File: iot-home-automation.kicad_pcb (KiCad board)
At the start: 4 copper layers, 53.2 x 41.6 mm, 26 parts, among them J1 Conn_01x05_Pin, J2 Conn_01x08_Pin, J3 Conn_01x02_Pin, J4 Conn_02x08_Odd_Even, Q1 PMOS, SW1 SW_Push_SPDT, U1 STM32WB5MMGH6TR, U2 SHTC3, U3 TPS62202DBV, U4 OPT3001DNPT

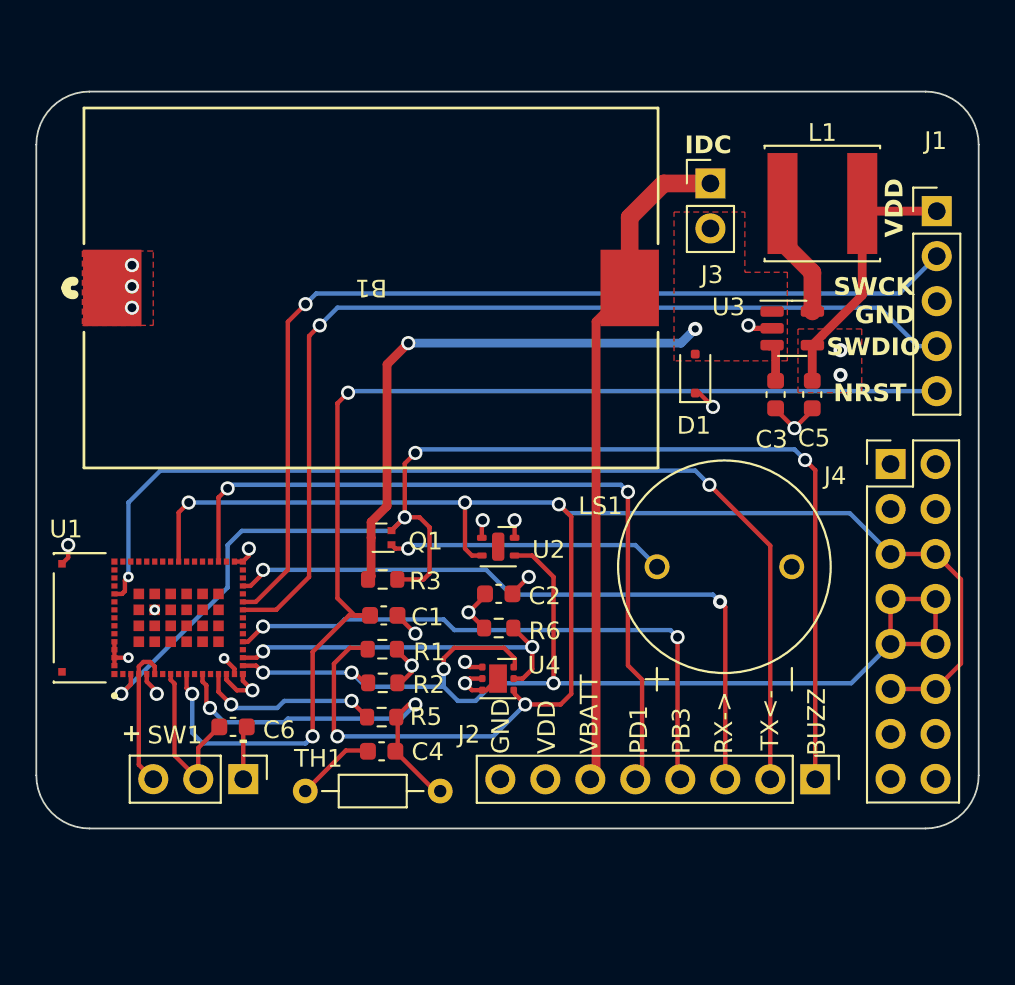
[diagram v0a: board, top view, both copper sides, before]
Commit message: Schematic and first routing pass done
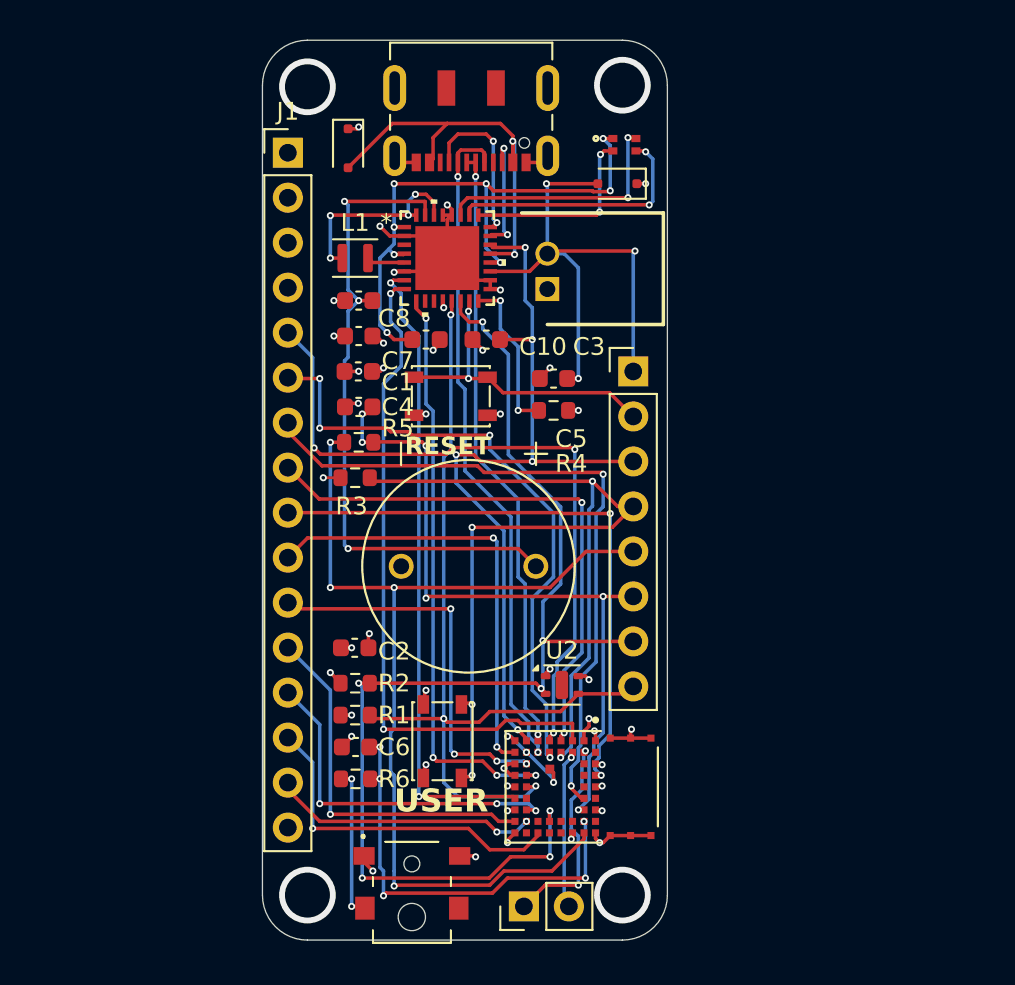
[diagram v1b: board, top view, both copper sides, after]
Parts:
- removed B1: BU2032SM-JJ-GTR, BU2032SM-JJ-GTR:BU2032SM-JJ-GTR_MPD
- removed J4: Conn_02x08_Odd_Even, Connector_PinHeader_2.54mm:PinHeader_2x08_P2.54mm_Vertical
- removed Q1: PMOS, Package_TO_SOT_SMD:SOT-723
- removed TH1: 3.3K@25C, Resistor_THT:R_Axial_DIN0204_L3.6mm_D1.6mm_P7.62mm_Horizontal
- removed U1: STM32WB5MMGH6TR, STM32WB5MMGH6TR:XCVR_STM32WB5MMGH6TR
- added C10: 10uF, Capacitor_SMD:C_0603_1608Metric, F.Cu at (140.8, 97.0)
- added C7: 0.1uF, Capacitor_SMD:C_0603_1608Metric, F.Cu at (137.0, 96.8)
- added C8: 1uF, Capacitor_SMD:C_0603_1608Metric, F.Cu at (137.0, 94.8)
- added D2: D_TVS, Diode_SMD:D_SOD-323F, F.Cu at (151.6, 88.2)
- added J5: Conn_01x02_Pin, Connector_PinHeader_2.54mm:PinHeader_1x02_P2.54mm_Vertical, F.Cu at (146.3, 129.0)
- added J6: Conn_01x08_Pin, Connector_PinHeader_2.54mm:PinHeader_1x08_P2.54mm_Vertical, F.Cu at (152.5, 98.8)
- added LED1: APHF1608LSEEQBDZGKC, ul_APHF1608LSEEQBDZGKC:APHF_KNB, F.Cu at (152.0, 86.0)
- added R4: 330K, Resistor_SMD:R_0603_1608Metric, F.Cu at (148.0, 101.0)
- added SW2: SW_Push, Button_Switch_SMD:SW_SPST_PTS810, F.Cu at (142.2, 100.2)
- added SW3: SW_Push, Button_Switch_SMD:SW_SPST_PTS810, F.Cu at (141.7, 119.7)
- C1: value 100nF -> 10uF
- C3: value 10u -> 1uF
- C4, C6: value 0.1u -> 100nF
- C5: value 10u -> 2.2uF
- J1: value Conn_01x05_Pin -> Conn_01x16_Female; footprint Connector_PinHeader_2.54mm:PinHeader_1x05_P2.54mm_Vertical -> Connector_PinHeader_2.54mm:PinHeader_1x16_P2.54mm_Vertical
- J2: value Conn_01x08_Pin -> USB_C_Receptacle_USB2.0_16P; footprint Connector_PinHeader_2.54mm:PinHeader_1x08_P2.54mm_Vertical -> Connector_USB:USB_C_Receptacle_JAE_DX07S016JA1R1500
- J3: value Conn_01x02_Pin -> 440055-2; footprint Connector_PinHeader_2.54mm:PinHeader_1x02_P2.54mm_Vertical -> jst:SHDRRA2W50P0X200_1X2_600X770X525P
- L1: value 10u -> 2.2uH; footprint Inductor_SMD:L_Changjiang_FNR6028S -> Inductor_SMD:L_Murata_DFE201610P
- R3: value 220K -> 10K
- R6: value 10K -> 200k
- SW1: footprint Connector_PinHeader_2.54mm:PinHeader_1x03_P2.54mm_Vertical -> CL-DA-1BB4-A2T:CLDA1BB4A2T
- U3: value TPS62202DBV -> 453-00059R; footprint Package_TO_SOT_SMD:SOT-23-5 -> 453-00059R:XCVR_453-00059R
- U4: value OPT3001DNPT -> NPM1300-QEAA-R7; footprint Package_SON:WSON-6-1EP_2x2mm_P0.65mm_EP1x1.6mm -> ul_NPM1300-QEAA-R7:QFN32_5X5_NOR
- moved J2 42.6 mm to (143.3, 84.0), turned to 180 degrees
- moved J1 36.8 mm to (133.0, 86.5)
- moved U3 28.5 mm to (149.6, 122.2), turned to -90 degrees
- moved L1 26.6 mm to (136.8, 92.4)
- moved U4 23.9 mm to (142.0, 92.4)
- moved D1 23.4 mm to (136.4, 86.2), turned to -90 degrees
- moved C4 19.5 mm to (137.0, 100.8)
- moved C3 16.6 mm to (144.2, 97.0), turned to 180 degrees
- moved R5 15.6 mm to (137.0, 102.8)
- moved C5 14.6 mm to (148.0, 99.2), turned to 180 degrees
- moved LS1 14.4 mm to (143.2, 109.8), turned to -90 degrees
- moved C1 13.8 mm to (137.0, 98.8), turned to 180 degrees
- moved R6 11.7 mm to (136.8, 121.8)
- moved SW1 11.5 mm to (140.0, 128.2), turned to 90 degrees
- moved J3 11.0 mm to (147.7, 94.2), turned to -90 degrees
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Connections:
- C1 pad 1: /NRST -> 3V3
- C2 pad 1: VDD -> 3V3
- C3 pad 1: VCC -> VBUSOUT
- C4 pad 1: /Vtherm -> /VTH
- C5 pad 1: VDD -> VBAT
- C6 pad 1: /Door_EXTI -> /Door_IRQ
- D1 pad 2: VCC -> VBUSIN
- J1 pad 1: VDD -> GND
- J1 pad 2: /SWCLK -> 3V3
- J1 pad 3: GND -> unconnected-(J1-Pin_3-Pad3)
- J1 pad 4: /SWDIO -> GND
- J1 pad 5: /NRST -> /IO14
- J3 pad 1: +BATT -> GND
- J3 pad 2: VCC -> VBAT
- L1 pad 1: Net-(U3-SW) -> 3V3
- L1 pad 2: VDD -> Net-(U4-SW2)
- LS1 pad P: Net-(Q1-D) -> /LSOUT2
- R1 pad 1: VDD -> 3V3
- R1 pad 2: /SCL1 -> /SDA
- R2 pad 1: VDD -> 3V3
- R2 pad 2: /SDA1 -> /SCL
- R3 pad 1: VCC -> 3V3
- R3 pad 2: /nBuzzer -> /USER_BTN
- R5 pad 1: /VDD_THERM -> /VDD_TH
- R5 pad 2: /Vtherm -> /VTH
- R6 pad 1: VDD -> Net-(SW1-B)
- R6 pad 2: /LIGHT_IRQ -> /Door_IRQ
- SW1 pad 2: /Door_EXTI -> Net-(SW1-B)
- SW1 pad 3: VDD -> 3V3
- U2 pad 1: VDD -> 3V3
- U2 pad 2: /SCL1 -> /SCL
- U2 pad 3: /SDA1 -> /SDA
- U3 pad 1: VCC -> GND
- U3 pad 2: GND -> unconnected-(U3-NC-Pad2)
- U3 pad 3: VCC -> GND
- U3 pad 4: VDD -> /IO24
- U3 pad 5: Net-(U3-SW) -> GND
- U4 pad 1: VDD -> VSYS
- U4 pad 3: GND -> unconnected-(U4-SW1-Pad3)
- U4 pad 4: /SCL1 -> VSYS
- U4 pad 5: /LIGHT_IRQ -> Net-(U4-SW2)
- U4 pad 6: /SDA1 -> GND
- U4 pad 7: GND -> /GPIO0
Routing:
- net /SCL1: track 94.7 -> 0.00 mm, vias 5 -> 0
- net /nBuzzer: track 74.6 -> 0.00 mm, vias 4 -> 0
- net /NRST: track 66.9 -> 0.00 mm, vias 3 -> 0
- net /SCL: track 0.00 -> 66.5 mm, vias 0 -> 7
- net /SDA1: track 65.4 -> 0.00 mm, vias 4 -> 0
- net /MCU_TX1: track 57.7 -> 0.00 mm, vias 2 -> 0
- net /USER_BTN: track 0.00 -> 56.9 mm, vias 0 -> 5
- net /VDD_TH: track 0.00 -> 56.1 mm, vias 0 -> 4
- net /SWCLK: track 55.5 -> 0.00 mm, vias 1 -> 0
- net /SDA: track 0.00 -> 49.6 mm, vias 0 -> 3
- net /SWDIO: track 55.1 -> 9.00 mm
- net VBUSOUT: track 0.00 -> 44.1 mm, vias 0 -> 5
- net /PD1: track 43.9 -> 0.00 mm, vias 2 -> 0
- net /VTH: track 0.00 -> 39.5 mm, vias 0 -> 6
- net /IO14: track 0.00 -> 39.2 mm, vias 0 -> 3
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- added copper zone on In2.Cu, net 3V3
- removed copper zone on F.Cu, net GND
- removed copper zone on F.Cu, net VCC
- removed copper zone on F.Cu, net VDD
- removed copper zone on In2.Cu, net VDD
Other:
- board size 53.2 x 41.6 mm -> 22.9 x 50.8 mm
- board text added: "RESET"
- board text added: "SWDCLK"
- board text added: "USER"
- board text removed: "+"
- board text removed: "-"
- board text removed: "BUZZ"
- board text removed: "GND"
- board text removed: "IDC"
- board text removed: "IoT Home Automation v1.0"
- board text removed: "NRST"
- board text removed: "PB3"
- board text removed: "PD1"
- board text removed: "RX->"
- board text removed: "SWCK"
- board text removed: "TX<-"
- board text removed: "VBATT"
- board text removed: "VDD"

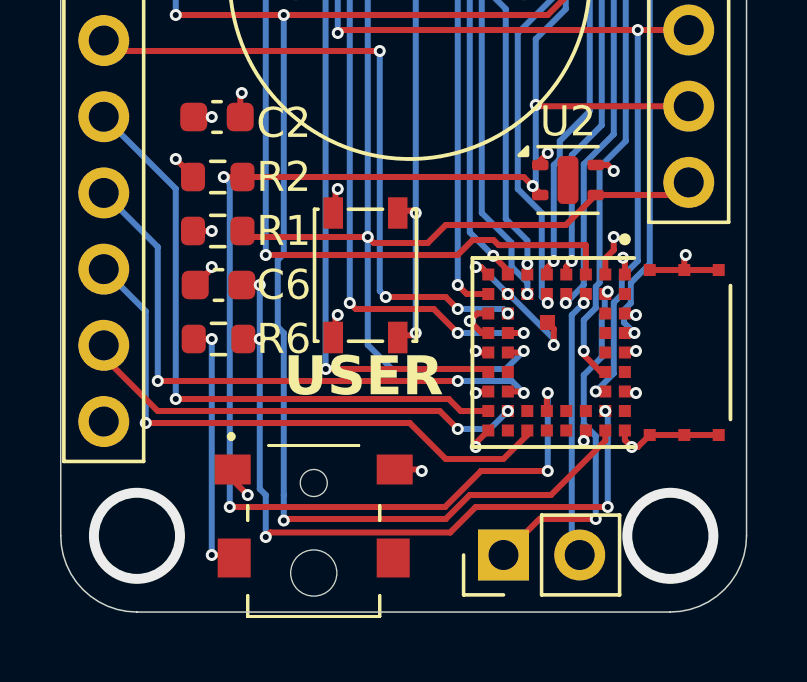
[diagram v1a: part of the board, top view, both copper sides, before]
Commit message: Limit switch placement fixed
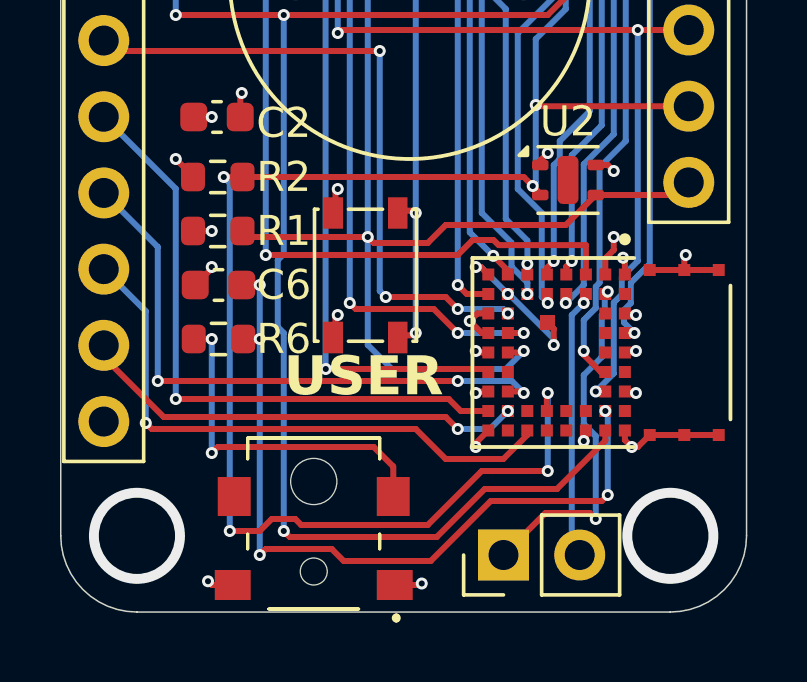
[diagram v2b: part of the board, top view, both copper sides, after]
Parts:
- moved SW1 0.25 mm to (140.0, 128.0), turned to -90 degrees
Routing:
- net Net-(SW1-B): track 8.59 -> 11.8 mm
- net /SCL: track 66.5 -> 67.8 mm
- net /Door_IRQ: track 24.7 -> 25.7 mm
- net /VDD_TH: track 56.1 -> 56.8 mm

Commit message: Rev A
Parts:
- removed C10: 10uF, Capacitor_SMD:C_0603_1608Metric
- removed C7: 0.1uF, Capacitor_SMD:C_0603_1608Metric
- added C11: 10uF, Capacitor_SMD:C_0603_1608Metric, F.Cu at (137.0, 96.8)
- added C9: 10uF, Capacitor_SMD:C_0603_1608Metric, F.Cu at (140.6, 97.0)
- C1: value 10uF -> 1uF
- C8: value 1uF -> 10uF
- moved C2 0.20 mm to (136.8, 114.6)
- turned C8 to 0 degrees
- turned L1 to 180 degrees
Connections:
- C1 pad 1: 3V3 -> /LSOUT2
- C8 pad 1: /LSOUT2 -> VSYS
- L1 pad 1: 3V3 -> Net-(U4-SW2)
- L1 pad 2: Net-(U4-SW2) -> +3V3
- U4 pad 12: 3V3 -> +3V3
- U4 pad 30: 3V3 -> +3V3
- U4 pad 32: 3V3 -> +3V3
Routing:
- net +3V3: track 0.00 -> 24.7 mm, vias 0 -> 7
- net 3V3: track 20.4 -> 8.60 mm, vias 15 -> 8
- net GND: track 47.0 -> 54.4 mm, vias 35 -> 32
- net VSYS: track 33.5 -> 39.7 mm, vias 8 -> 9
- net /LED1: track 14.5 -> 15.9 mm
- net /GPIO0: track 36.0 -> 37.3 mm, vias 2 -> 4
- net /LED2: track 14.1 -> 14.9 mm
- net VBUSIN: track 23.8 -> 24.5 mm
- net /SCL: track 67.8 -> 68.5 mm
- net /SWDCLK: track 11.9 -> 11.2 mm
- net /LED0: track 11.0 -> 11.7 mm
- net /VDD_TH: track 56.8 -> 57.3 mm
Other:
- board text added: "3V3"
- board text added: "GND"
- board text added: "IO14"
- board text added: "IO15"
- board text added: "IO16"
- board text added: "IO17"
- board text added: "IO24"
- board text added: "IO25"
- board text added: "MISO"
- board text added: "MOSI"
- board text added: "RX"
- board text added: "SCK"
- board text added: "SCL"
- board text added: "SDA"
- board text added: "TX"
- board text added: "USER_BTN"
- board text added: "VBAT"
- board text added: "VBUS"
- board text added: "VDD_TH"
- board text added: "VTH"

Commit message: RevB done?
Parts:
- removed C6: 100nF, Capacitor_SMD:C_0603_1608Metric
- removed R6: 200k, Resistor_SMD:R_0603_1608Metric
- removed SW1: SW_Push_SPDT, CL-DA-1BB4-A2T:CLDA1BB4A2T
- added S1: CL-DA-1BB4-A2T, CL-DA-1BB4-A2T:CLDA1BB4A2T, F.Cu at (140.1, 128.2)
- added TP1: TestPoint, TestPoint:TestPoint_Pad_D1.5mm, B.Cu at (142.0, 83.0)
- added TP2: TestPoint, TestPoint:TestPoint_Pad_D1.5mm, B.Cu at (144.8, 83.0)
- C2, C4: value 100nF -> 0.1uF
- C5: value 2.2uF -> 10uF
- moved R3 17.2 mm to (136.8, 122.0)
- moved J3 0.40 mm to (148.1, 94.2)
- moved J2 0.35 mm to (143.3, 83.6)
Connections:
- C2 pad 1: 3V3 -> +3V3
- J1 pad 2: 3V3 -> +3V3
- J1 pad 3: unconnected-(J1-Pin_3-Pad3) -> +3V3
- J1 pad 9: /IO24 -> /LSOUT2
- J6 pad 2: /SHPHLD -> VBUSOUT
- J6 pad 3: VBUSOUT -> GND
- J6 pad 4: /USER_BTN -> +3V3
- R1 pad 1: 3V3 -> +3V3
- R2 pad 1: 3V3 -> +3V3
- R3 pad 1: 3V3 -> +3V3
- U2 pad 1: 3V3 -> +3V3
- U3 pad 12: unconnected-(U3-SIO_31/AIN7-Pad12) -> /DOOR_SW
- U3 pad 21: 3V3 -> +3V3
- U3 pad 22: 3V3 -> +3V3
- U3 pad 30: 3V3 -> +3V3
- U3 pad 37: /Door_IRQ -> unconnected-(U3-SIO_02/AIN0-Pad37)
- U3 pad 4: /IO24 -> unconnected-(U3-SIO_24-Pad4)
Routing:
- net /IO24: track 33.8 -> 0.00 mm, vias 2 -> 0
- net /USER_BTN: track 56.9 -> 28.0 mm
- net /Door_IRQ: track 25.9 -> 0.00 mm, vias 5 -> 0
- net Net-(SW1-B): track 11.8 -> 0.00 mm, vias 2 -> 0
- net /DOOR_SW: track 0.00 -> 10.7 mm, vias 0 -> 2
- net /SHPHLD: track 17.9 -> 8.61 mm
- net GND: track 54.4 -> 45.6 mm, vias 32 -> 38
- net 3V3: track 8.60 -> 0.00 mm, vias 8 -> 0
- net /D-: track 37.9 -> 45.6 mm
- net +3V3: track 24.7 -> 31.2 mm, vias 7 -> 14
- net /D+: track 34.6 -> 40.1 mm
- net /LSOUT2: track 37.9 -> 41.1 mm, vias 3 -> 4
- net /VDD_TH: track 57.3 -> 54.2 mm
- net /IO15: track 35.3 -> 37.6 mm
- net /SCK: track 21.9 -> 23.5 mm
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- added copper zone on In2.Cu, net +3V3
- removed copper zone on In2.Cu, net 3V3
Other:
- board text added: "LSOUT2"
- board text added: "SIO"
- board text added: "SWC"
- board text added: "TH+"
- board text added: "TH-"
- board text removed: "IO24"
- board text removed: "SWDCLK"
- board text removed: "SWDIO"
- board text removed: "USER_BTN"
- board text removed: "VDD_TH"
- board text removed: "VTH"
